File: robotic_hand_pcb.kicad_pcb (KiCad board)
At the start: 4 copper layers, 0 parts

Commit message: Fix symbol error, update component_library
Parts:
- added C1: 100n, Capacitor_SMD:C_0603_1608Metric, F.Cu at (26.0, 46.5)
- added C10: 100n, Capacitor_SMD:C_0603_1608Metric, F.Cu at (30.0, 51.5)
- added C11: 100n, Capacitor_SMD:C_0603_1608Metric, F.Cu at (30.0, 54.0)
- added C12: 100n, Capacitor_SMD:C_0603_1608Metric, F.Cu at (30.0, 56.5)
- added C13: 4u7, Capacitor_SMD:C_0603_1608Metric, F.Cu at (30.0, 59.1)
- added C14: 100n, Capacitor_SMD:C_0603_1608Metric, F.Cu at (30.0, 61.6)
- added C15: 30p, Capacitor_SMD:C_0402_1005Metric, F.Cu at (51.9, 46.2)
- added C16: 30p, Capacitor_SMD:C_0402_1005Metric, F.Cu at (51.9, 48.2)
- added C17: 2u2, Capacitor_SMD:C_0603_1608Metric, F.Cu at (34.0, 46.5)
- added C18: 18p, Capacitor_SMD:C_0402_1005Metric, F.Cu at (51.9, 50.2)
- added C19: 18p, Capacitor_SMD:C_0402_1005Metric, F.Cu at (51.9, 52.1)
- added C2: 2u2, Capacitor_SMD:C_0603_1608Metric, F.Cu at (26.0, 49.0)
- added C20: 100n, Capacitor_SMD:C_0603_1608Metric, F.Cu at (97.3, 18.1)
- added C21: 100n, Capacitor_SMD:C_0603_1608Metric, F.Cu at (97.3, 20.6)
- added C22: 18p, Capacitor_SMD:C_0402_1005Metric, F.Cu at (100.8, 31.0)
- added C23: 18p, Capacitor_SMD:C_0402_1005Metric, F.Cu at (100.8, 33.0)
- added C24: 100n, Capacitor_SMD:C_0603_1608Metric, F.Cu at (97.3, 23.1)
- added C25: 100n, Capacitor_SMD:C_0603_1608Metric, F.Cu at (70.7, 35.0)
- added C26: 100n, Capacitor_SMD:C_0603_1608Metric, F.Cu at (70.7, 37.5)
- added C27: 1u, Capacitor_SMD:C_0603_1608Metric, F.Cu at (70.7, 40.0)
- added C28: 100n, Capacitor_SMD:C_0603_1608Metric, F.Cu at (70.7, 42.5)
- added C29: 100n, Capacitor_SMD:C_0603_1608Metric, F.Cu at (70.7, 45.0)
- added C3: 22u, Capacitor_SMD:C_0603_1608Metric, F.Cu at (26.0, 51.5)
- added C30: 100n, Capacitor_SMD:C_0603_1608Metric, F.Cu at (74.7, 35.0)
- added C31: 100n, Capacitor_SMD:C_0603_1608Metric, F.Cu at (74.7, 37.5)
- added C32: 100n, Capacitor_SMD:C_0603_1608Metric, F.Cu at (74.7, 40.0)
- added C33: 1n, Capacitor_SMD:C_0603_1608Metric, F.Cu at (74.7, 42.5)
- added C34: 1n, Capacitor_SMD:C_0603_1608Metric, F.Cu at (74.7, 45.0)
- added C35: 1n, Capacitor_SMD:C_0603_1608Metric, F.Cu at (78.7, 35.0)
- added C36: 1n, Capacitor_SMD:C_0603_1608Metric, F.Cu at (78.7, 37.5)
- added C37: 1n, Capacitor_SMD:C_0603_1608Metric, F.Cu at (78.7, 40.0)
- added C38: 100n, Capacitor_SMD:C_0603_1608Metric, F.Cu at (41.3, 29.7)
- added C39: 100n, Capacitor_SMD:C_0603_1608Metric, F.Cu at (41.3, 32.2)
- added C4: 44u, Capacitor_SMD:C_0603_1608Metric, F.Cu at (26.0, 54.0)
- added C40: 100n, Capacitor_SMD:C_0603_1608Metric, F.Cu at (41.3, 34.7)
- added C41: 100n, Capacitor_SMD:C_0603_1608Metric, F.Cu at (41.3, 37.2)
- added C42: 100n, Capacitor_SMD:C_0603_1608Metric, F.Cu at (41.3, 39.7)
- added C5: 1u, Capacitor_SMD:C_0603_1608Metric, F.Cu at (26.0, 56.5)
- added C6: 2u2, Capacitor_SMD:C_0603_1608Metric, F.Cu at (26.0, 59.1)
- added C7: 100n, Capacitor_SMD:C_0603_1608Metric, F.Cu at (26.0, 61.6)
- added C8: 100n, Capacitor_SMD:C_0603_1608Metric, F.Cu at (30.0, 46.5)
- added C9: 100n, Capacitor_SMD:C_0603_1608Metric, F.Cu at (30.0, 49.0)
- added D1: WS2812B, LED_SMD:LED_WS2812B_PLCC4_5.0x5.0mm_P3.2mm, F.Cu at (95.3, 64.7)
- added D2: WS2812B, LED_SMD:LED_WS2812B_PLCC4_5.0x5.0mm_P3.2mm, F.Cu at (95.3, 71.4)
- added D3: WS2812B, LED_SMD:LED_WS2812B_PLCC4_5.0x5.0mm_P3.2mm, F.Cu at (95.3, 78.0)
- added D4: WS2812B, LED_SMD:LED_WS2812B_PLCC4_5.0x5.0mm_P3.2mm, F.Cu at (95.3, 84.6)
- added FM1: 1mm, Fiducial:Fiducial_1mm_Mask2mm, F.Cu at (37.9, 76.1)
- added FM2: 1mm, Fiducial:Fiducial_1mm_Mask2mm, F.Cu at (37.9, 79.6)
- added FM3: 1mm, Fiducial:Fiducial_1mm_Mask2mm, F.Cu at (41.4, 76.1)
- added FM4: 1mm, Fiducial:Fiducial_1mm_Mask2mm, F.Cu at (41.4, 79.6)
- added FM5: 1mm, Fiducial:Fiducial_1mm_Mask2mm, F.Cu at (45.0, 76.1)
- added FM6: 1mm, Fiducial:Fiducial_1mm_Mask2mm, F.Cu at (45.0, 79.6)
- added H1: M3, MountingHole:MountingHole_3.2mm_M3_Pad_Via, F.Cu at (20.0, 49.2)
- added H2: M3, MountingHole:MountingHole_3.2mm_M3_Pad_Via, F.Cu at (20.0, 57.2)
- added H3: M3, MountingHole:MountingHole_3.2mm_M3_Pad_Via, F.Cu at (20.0, 65.1)
- added H4: M3, MountingHole:MountingHole_3.2mm_M3_Pad_Via, F.Cu at (20.0, 73.1)
- added J1: 2171750001, common:molex_2171750001_usb_c_6p, F.Cu at (29.8, 75.8)
- added J10: A5, Connector_PinHeader_2.54mm:PinHeader_1x03_P2.54mm_Vertical, F.Cu at (81.2, 19.2)
- added J11: A6, Connector_PinHeader_2.54mm:PinHeader_1x03_P2.54mm_Vertical, F.Cu at (85.8, 19.2)
- added J12: A7, Connector_PinHeader_2.54mm:PinHeader_1x03_P2.54mm_Vertical, F.Cu at (90.5, 19.2)
- added J13: ISENSE1, Connector_PinHeader_2.54mm:PinHeader_1x02_P2.54mm_Vertical, F.Cu at (71.0, 28.9)
- added J14: ISENSE2, Connector_PinHeader_2.54mm:PinHeader_1x02_P2.54mm_Vertical, F.Cu at (75.7, 28.9)
- added J15: ISENSE3, Connector_PinHeader_2.54mm:PinHeader_1x02_P2.54mm_Vertical, F.Cu at (80.3, 28.9)
- added J16: ISENSE4, Connector_PinHeader_2.54mm:PinHeader_1x02_P2.54mm_Vertical, F.Cu at (85.0, 28.9)
- added J17: ISENSE5, Connector_PinHeader_2.54mm:PinHeader_1x02_P2.54mm_Vertical, F.Cu at (89.6, 28.9)
- added J18: JST 1x5 Male, Connector_PinHeader_2.54mm:PinHeader_1x05_P2.54mm_Vertical, F.Cu at (18.3, 30.8)
- added J19: JST 1x5 Male, Connector_PinHeader_2.54mm:PinHeader_1x05_P2.54mm_Vertical, F.Cu at (23.0, 30.8)
- added J2: TC2050-IDC, tag_connect:tag_connect_tc2050-idc, F.Cu at (41.7, 68.6)
- added J20: JST 1x5 Male, Connector_PinHeader_2.54mm:PinHeader_1x05_P2.54mm_Vertical, F.Cu at (27.6, 30.8)
- added J21: JST 1x5 Male, Connector_PinHeader_2.54mm:PinHeader_1x05_P2.54mm_Vertical, F.Cu at (32.3, 30.8)
- added J22: JST 1x5 Male, Connector_PinHeader_2.54mm:PinHeader_1x05_P2.54mm_Vertical, F.Cu at (36.9, 30.8)
- added J3: ~, common:harwin_2p_2-54_jumper_open, F.Cu at (19.7, 79.5)
- added J4: UART, Connector_PinHeader_2.54mm:PinHeader_1x02_P2.54mm_Vertical, F.Cu at (52.8, 55.5)
- added J5: WS2812B, Connector_PinHeader_2.54mm:PinHeader_1x03_P2.54mm_Vertical, F.Cu at (101.7, 63.8)
- added J6: A1, Connector_PinHeader_2.54mm:PinHeader_1x03_P2.54mm_Vertical, F.Cu at (62.6, 19.2)
- added J7: A2, Connector_PinHeader_2.54mm:PinHeader_1x03_P2.54mm_Vertical, F.Cu at (67.2, 19.2)
- added J8: A3, Connector_PinHeader_2.54mm:PinHeader_1x03_P2.54mm_Vertical, F.Cu at (71.9, 19.2)
- added J9: A4, Connector_PinHeader_2.54mm:PinHeader_1x03_P2.54mm_Vertical, F.Cu at (76.5, 19.2)
- added JP1: Open, Jumper:SolderJumper-2_P1.3mm_Open_TrianglePad1.0x1.5mm, F.Cu at (66.9, 84.6)
- added JP2: Open, Jumper:SolderJumper-2_P1.3mm_Open_TrianglePad1.0x1.5mm, F.Cu at (101.5, 28.3)
- added L1: 6u8, Resistor_SMD:R_0603_1608Metric, F.Cu at (34.0, 49.0)
- added R1: 100k, Resistor_SMD:R_0603_1608Metric, F.Cu at (34.0, 51.5)
- added R10: 2k2, Resistor_SMD:R_0603_1608Metric, F.Cu at (97.3, 35.7)
- added R2: 13k7, Resistor_SMD:R_0603_1608Metric, F.Cu at (34.0, 54.0)
- added R3: 5k1, Resistor_SMD:R_0603_1608Metric, F.Cu at (34.0, 56.5)
- added R4: 5k1, Resistor_SMD:R_0603_1608Metric, F.Cu at (34.0, 59.1)
- added R5: 10k, Resistor_SMD:R_0603_1608Metric, F.Cu at (34.0, 61.6)
- added R6: 10k, Resistor_SMD:R_0603_1608Metric, F.Cu at (97.3, 25.6)
- added R7: 10k, Resistor_SMD:R_0603_1608Metric, F.Cu at (97.3, 28.1)
- added R8: 10k, Resistor_SMD:R_0603_1608Metric, F.Cu at (97.3, 30.6)
- added R9: 2k2, Resistor_SMD:R_0603_1608Metric, F.Cu at (97.3, 33.1)
- added SW1: SPST, Button_Switch_THT:SW_PUSH_6mm, F.Cu at (48.8, 76.3)
- added TP1: TestPoint, TestPoint:TestPoint_Pad_D2.0mm, F.Cu at (82.8, 35.8)
- added TP2: TestPoint, TestPoint:TestPoint_Pad_D2.0mm, F.Cu at (82.8, 39.8)
- added TP3: TestPoint, TestPoint:TestPoint_Pad_D2.0mm, F.Cu at (82.8, 43.9)
- added TP4: TestPoint, TestPoint:TestPoint_Pad_D2.0mm, F.Cu at (82.8, 47.9)
- added TP5: TestPoint, TestPoint:TestPoint_Pad_D2.0mm, F.Cu at (82.8, 52.0)
- added U1: LMR51430, ti_buck:lmr51430, F.Cu at (27.3, 82.5)
- added U10: ACS712xLCTR-05B, Package_SO:SOIC-8_3.9x4.9mm_P1.27mm, F.Cu at (64.5, 36.5)
- added U11: ACS712xLCTR-05B, Package_SO:SOIC-8_3.9x4.9mm_P1.27mm, F.Cu at (64.5, 43.0)
- added U12: ACS712xLCTR-05B, Package_SO:SOIC-8_3.9x4.9mm_P1.27mm, F.Cu at (64.5, 49.6)
- added U13: ACS712xLCTR-05B, Package_SO:SOIC-8_3.9x4.9mm_P1.27mm, F.Cu at (64.5, 56.2)
- added U14: ULN2003ADR, Package_SO:SOIC-16_3.9x9.9mm_P1.27mm, F.Cu at (20.2, 22.7)
- added U15: ULN2003ADR, Package_SO:SOIC-16_3.9x9.9mm_P1.27mm, F.Cu at (28.7, 22.7)
- added U16: ULN2003ADR, Package_SO:SOIC-16_3.9x9.9mm_P1.27mm, F.Cu at (37.1, 22.7)
- added U17: ULN2003ADR, Package_SO:SOIC-16_3.9x9.9mm_P1.27mm, F.Cu at (45.6, 22.7)
- added U18: ULN2003ADR, Package_SO:SOIC-16_3.9x9.9mm_P1.27mm, F.Cu at (54.0, 22.7)
- added U2: ld39150dt33-r, common:to-252-2_dpak-2-leg, F.Cu at (30.9, 66.9)
- added U3: TXB0104QPWRQ1, common:txb0104qpwrq1, F.Cu at (51.5, 66.2)
- added U4: STM32F446RET, Package_QFP:LQFP-64_10x10mm_P0.5mm, F.Cu at (43.2, 52.5)
- added U5: VL53L4CD, time_of_flight:vl53l4cd_lga12, F.Cu at (62.3, 85.8)
- added U6: ~, adafruit:adafruit_5396_vl53l4cd, F.Cu at (74.7, 72.1)
- added U7: BNO085, ceva:bno085, F.Cu at (101.9, 20.1)
- added U8: ADS114S08, adc:ads114s08_tqfp-32, F.Cu at (89.1, 38.0)
- added U9: ACS712xLCTR-05B, Package_SO:SOIC-8_3.9x4.9mm_P1.27mm, F.Cu at (64.5, 29.9)
- added Y1: 8M, common:ecs_ecx-64, F.Cu at (51.6, 71.7)
- added Y2: 32k768, common:ecs_ecx-34r, F.Cu at (33.0, 81.8)
- added Y3: 32k768, common:ecs_ecx-34r, F.Cu at (102.3, 24.9)

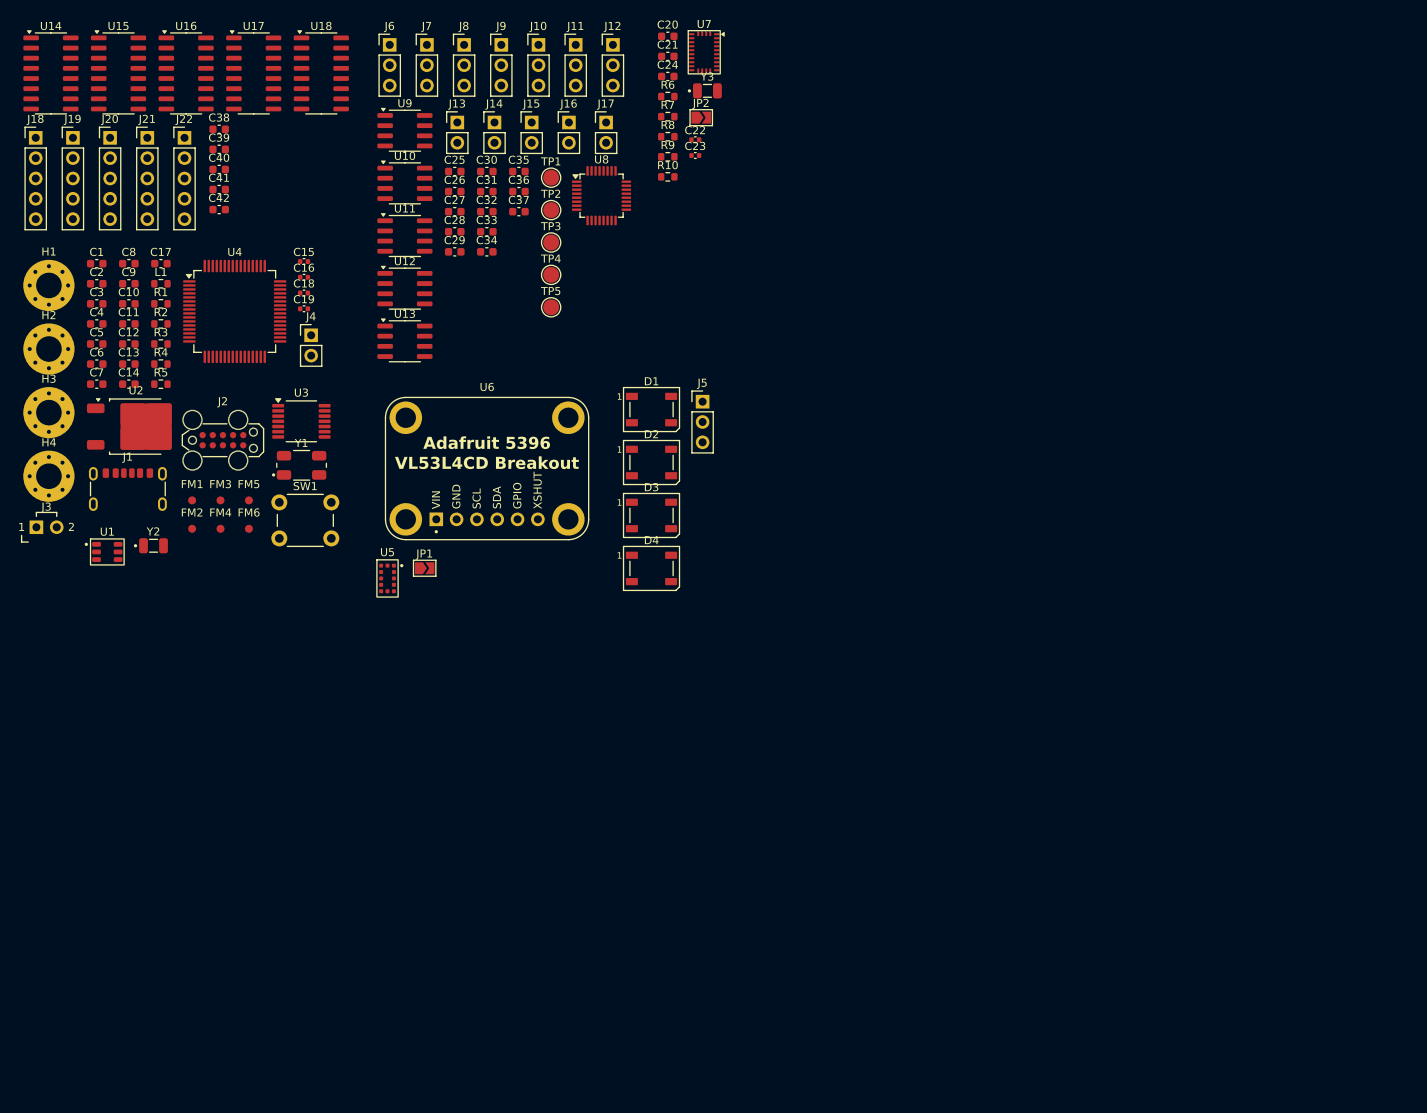
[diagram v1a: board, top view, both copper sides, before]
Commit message: Add WIP PCB layout and routing
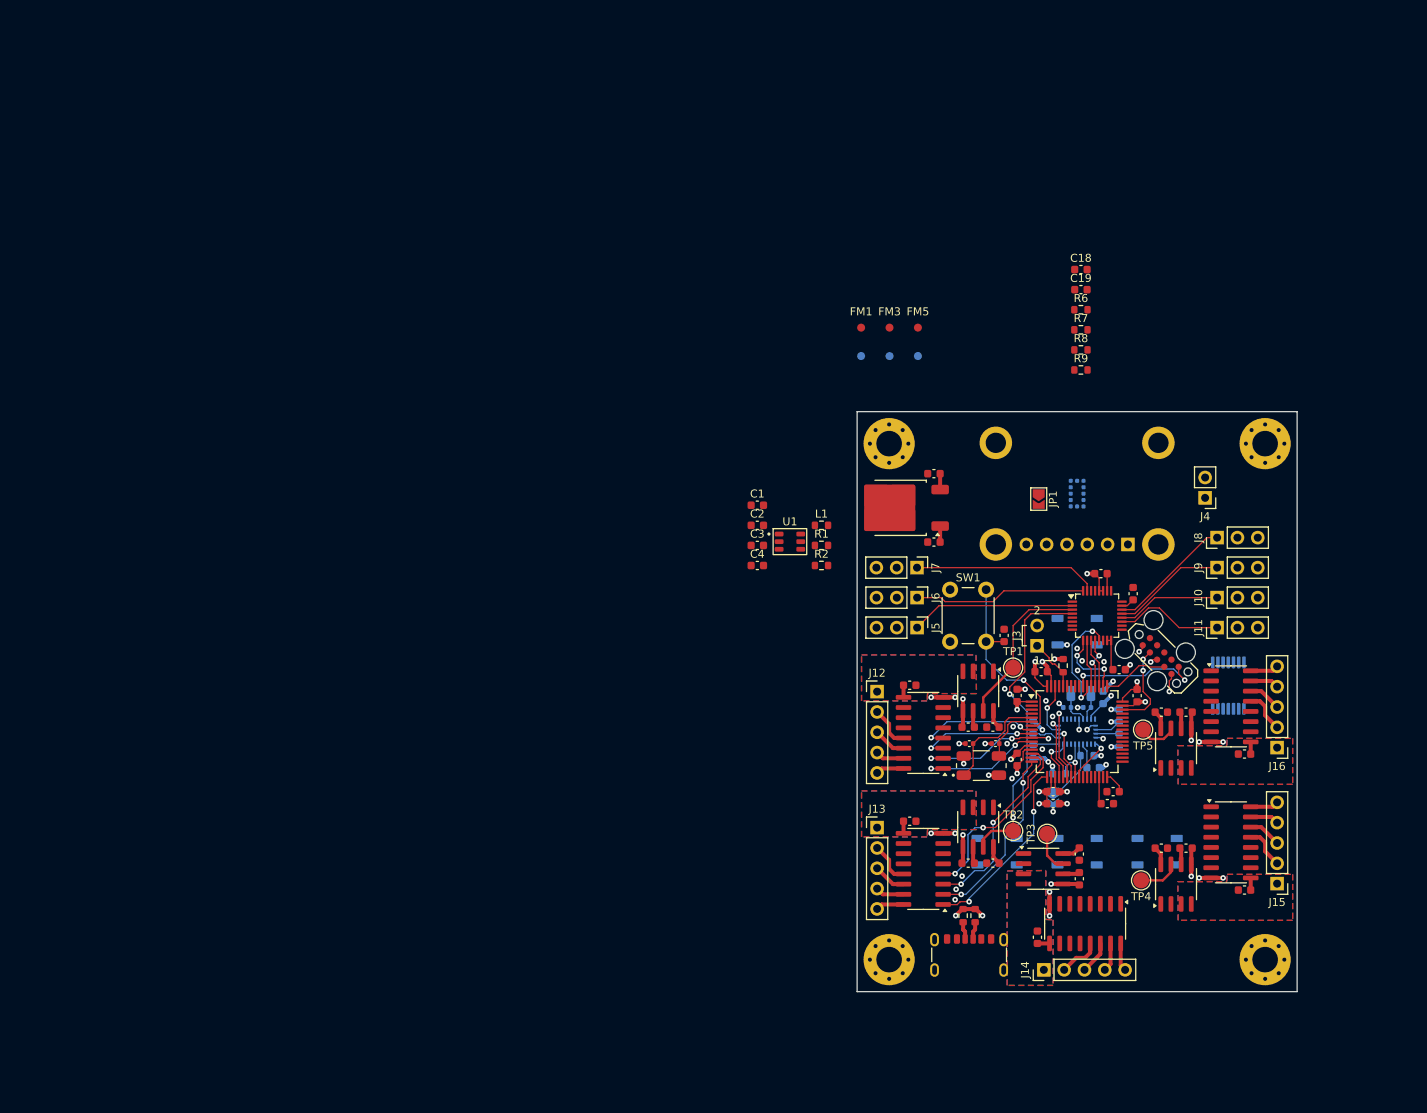
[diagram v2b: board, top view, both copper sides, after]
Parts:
- removed the C38 at (41.3, 29.7)
- removed J17: ISENSE5, Connector_PinHeader_2.54mm:PinHeader_1x02_P2.54mm_Vertical
- removed J18, J19, J20, J21: JST 1x5 Male, Connector_PinHeader_2.54mm:PinHeader_1x05_P2.54mm_Vertical
- removed the J5 at (101.7, 63.8)
- removed the U14 at (20.2, 22.7)
- removed the Y2 at (33.0, 81.8)
- added C42: 100n, Capacitor_SMD:C_0603_1608Metric, F.Cu at (169.4, 107.8)
- added R6: 2k2, Resistor_SMD:R_0603_1608Metric, F.Cu at (149.0, 52.3)
- added R7: 2k2, Resistor_SMD:R_0603_1608Metric, F.Cu at (149.0, 54.8)
- added R8: 2k2, Resistor_SMD:R_0603_1608Metric, F.Cu at (149.0, 57.3)
- added R9: 2k2, Resistor_SMD:R_0603_1608Metric, F.Cu at (149.0, 59.8)
- added U18: ULN2003ADR, Package_SO:SOIC-16_3.9x9.9mm_P1.27mm, F.Cu at (167.7, 101.8)
- C18: value 18p -> 100n; footprint Capacitor_SMD:C_0402_1005Metric -> Capacitor_SMD:C_0603_1608Metric
- C19: value 18p -> 4u7; footprint Capacitor_SMD:C_0402_1005Metric -> Capacitor_SMD:C_0603_1608Metric
- C20, C21, C22, C23, C24, D1, D2, D3, D4, FM2, FM4, FM6, JP2, U3, U5, U6, U7: moved to B.Cu
- J10: renamed from J12; value A7 -> A6
- J11: value A6 -> A7
- J13: value ISENSE1 -> JST 1x5 Male; footprint Connector_PinHeader_2.54mm:PinHeader_1x02_P2.54mm_Vertical -> Connector_PinHeader_2.54mm:PinHeader_1x05_P2.54mm_Vertical
- J14: value ISENSE2 -> JST 1x5 Male; footprint Connector_PinHeader_2.54mm:PinHeader_1x02_P2.54mm_Vertical -> Connector_PinHeader_2.54mm:PinHeader_1x05_P2.54mm_Vertical
- J15: value ISENSE3 -> JST 1x5 Male; footprint Connector_PinHeader_2.54mm:PinHeader_1x02_P2.54mm_Vertical -> Connector_PinHeader_2.54mm:PinHeader_1x05_P2.54mm_Vertical
- J16: value ISENSE4 -> JST 1x5 Male; footprint Connector_PinHeader_2.54mm:PinHeader_1x02_P2.54mm_Vertical -> Connector_PinHeader_2.54mm:PinHeader_1x05_P2.54mm_Vertical
- R10: renamed from R6; moved to B.Cu
- R11: renamed from R7; moved to B.Cu
- R12: renamed from R8; moved to B.Cu
- R13: renamed from R9; moved to B.Cu
- R14: renamed from R10; moved to B.Cu
- Y2: renamed from Y3; moved to B.Cu
- moved H3 166.7 mm to (172.0, 133.5)
- moved U17 155.4 mm to (167.7, 118.8)
- moved C41 155.2 mm to (169.4, 124.8), turned to 180 degrees
- moved U16 154.7 mm to (149.5, 129.0), turned to -90 degrees
- moved H2 152.5 mm to (172.0, 69.0)
- moved U15 141.4 mm to (129.3, 122.2), turned to 180 degrees
- moved C40 140.3 mm to (143.5, 130.7), turned to 90 degrees
- moved C9 138.4 mm to (153.0, 112.5), turned to 180 degrees
- moved C17 136.2 mm to (152.3, 114.0)
- moved C10 135.2 mm to (156.0, 100.5), turned to -90 degrees
- moved J15 133.2 mm to (173.5, 124.0), turned to 180 degrees
- moved C8 133.1 mm to (145.5, 112.5), turned to 180 degrees
- moved C13 127.9 mm to (145.5, 114.0), turned to 180 degrees
- moved J14 126.2 mm to (144.3, 134.8), turned to 90 degrees
- moved J3 124.6 mm to (143.5, 93.0), turned to 90 degrees
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- renumbered C42 to C38, J22 to J12, J6 to J5, J7 to J6, J8 to J7, J9 to J8, J10 to J9, U18 to U14
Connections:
- C18 pad 1: /LSE_IN -> +3V3
- C19 pad 1: /LSE_OUT -> +3V3
- D4 pad 2: Net-(D4-DOUT) -> unconnected-(D4-DOUT-Pad2)
- J10 pad 1: /robotic_hand_pcb_analog/ADC12 -> /robotic_hand_pcb_analog/ADC11
- J11 pad 1: /robotic_hand_pcb_analog/ADC11 -> /robotic_hand_pcb_analog/ADC12
- J12 pad 2: Net-(J22-Pin_2) -> Net-(J12-Pin_2)
- J12 pad 3: Net-(J22-Pin_3) -> Net-(J12-Pin_3)
- J12 pad 4: Net-(J22-Pin_4) -> Net-(J12-Pin_4)
- J12 pad 5: Net-(J22-Pin_5) -> Net-(J12-Pin_5)
- J13 pad 2: +5V -> Net-(J13-Pin_2)
- J14 pad 2: +5V -> Net-(J14-Pin_2)
- J15 pad 2: +5V -> Net-(J15-Pin_2)
- J16 pad 2: +5V -> Net-(J16-Pin_2)
- U14 pad 1: /M5_1 -> /M1_1
- U14 pad 13: Net-(J22-Pin_5) -> Net-(J12-Pin_2)
- U14 pad 14: Net-(J22-Pin_4) -> Net-(J12-Pin_3)
- U14 pad 15: Net-(J22-Pin_3) -> Net-(J12-Pin_4)
- U14 pad 16: Net-(J22-Pin_2) -> Net-(J12-Pin_5)
- U14 pad 2: /M5_2 -> /M1_2
- U14 pad 3: /M5_3 -> /M1_3
- U14 pad 4: /M5_4 -> /M1_4
- U15 pad 1: /M2_1 -> /M3_1
- U15 pad 13: Net-(J19-Pin_5) -> Net-(J13-Pin_2)
- U15 pad 14: Net-(J19-Pin_4) -> Net-(J13-Pin_3)
- U15 pad 15: Net-(J19-Pin_3) -> Net-(J13-Pin_4)
- U15 pad 16: Net-(J19-Pin_2) -> Net-(J13-Pin_5)
- U15 pad 2: /M2_2 -> /M3_2
- U15 pad 3: /M2_3 -> /M3_3
- U15 pad 4: /M2_4 -> /M3_4
- U16 pad 1: /M3_1 -> /M4_1
- U16 pad 13: Net-(J20-Pin_5) -> Net-(J14-Pin_2)
- U16 pad 14: Net-(J20-Pin_4) -> Net-(J14-Pin_3)
- U16 pad 15: Net-(J20-Pin_3) -> Net-(J14-Pin_4)
- U16 pad 16: Net-(J20-Pin_2) -> Net-(J14-Pin_5)
- U16 pad 2: /M3_2 -> /M4_2
- U16 pad 3: /M3_3 -> /M4_3
- U16 pad 4: /M3_4 -> /M4_4
- U17 pad 1: /M4_1 -> /M5_1
- U17 pad 13: Net-(J21-Pin_5) -> Net-(J15-Pin_2)
- U17 pad 14: Net-(J21-Pin_4) -> Net-(J15-Pin_3)
- U17 pad 15: Net-(J21-Pin_3) -> Net-(J15-Pin_4)
- U17 pad 16: Net-(J21-Pin_2) -> Net-(J15-Pin_5)
- U17 pad 2: /M4_2 -> /M5_2
- U17 pad 3: /M4_3 -> /M5_3
- U17 pad 4: /M4_4 -> /M5_4
- U4 pad 10: /M1_3 -> /M1_2
- U4 pad 11: /M1_4 -> /M1_1
- U4 pad 14: /M3_1 -> /M3_4
- U4 pad 15: /M3_2 -> /M3_3
- U4 pad 16: /M3_3 -> /M3_2
- U4 pad 17: /EXTI3_IMU_INT -> /M3_1
- U4 pad 20: /GPIO_SPI1_CS -> /EXTI4_IMU_INT
- U4 pad 26: /M3_4 -> /M4_4
- U4 pad 27: /M4_1 -> /M4_3
- U4 pad 29: unconnected-(U4-PB10-Pad29) -> /M4_1
- U4 pad 3: /LSE_IN -> unconnected-(U4-PC14_OSC32_LSE_IN-Pad3)
- U4 pad 33: /M5_1 -> /M5_4
- U4 pad 34: /M5_2 -> /M5_3
- U4 pad 35: /M5_3 -> /M5_2
- U4 pad 36: /M5_4 -> /M5_1
- U4 pad 37: /M2_1 -> /M2_4
- U4 pad 38: /M2_2 -> /M2_3
- U4 pad 39: /M2_3 -> /M2_2
- U4 pad 4: /LSE_OUT -> unconnected-(U4-PC15_OSC32_LSE_OUT-Pad4)
- U4 pad 40: /M2_4 -> /M2_1
- U4 pad 61: /M4_3 -> unconnected-(U4-PB8-Pad61)
- U4 pad 62: /M4_4 -> /GPIO_SPI1_CS
- U4 pad 8: /M1_1 -> /M1_4
- U4 pad 9: /M1_2 -> /M1_3
- U7 pad 14: /EXTI3_IMU_INT -> /EXTI4_IMU_INT
- U8 pad 3: /robotic_hand_pcb_analog/ADC5 -> /robotic_hand_pcb_analog/ADC1
- U8 pad 4: /robotic_hand_pcb_analog/ADC4 -> /robotic_hand_pcb_analog/ADC2
- U8 pad 6: /robotic_hand_pcb_analog/ADC2 -> /robotic_hand_pcb_analog/ADC4
- U8 pad 7: /robotic_hand_pcb_analog/ADC1 -> /robotic_hand_pcb_analog/ADC5
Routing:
- net GND: track 0.00 -> 76.1 mm, vias 0 -> 55
- net +3V3: track 0.00 -> 44.6 mm, vias 0 -> 15
- net /robotic_hand_pcb_analog/ADC2: track 0.00 -> 40.2 mm, vias 0 -> 2
- net /NRST: track 0.00 -> 24.2 mm, vias 0 -> 1
- net /M3_3: track 0.00 -> 23.8 mm, vias 0 -> 2
- net /M3_4: track 0.00 -> 23.6 mm, vias 0 -> 2
- net /M3_1: track 0.00 -> 23.4 mm, vias 0 -> 2
- net +5V: track 0.00 -> 23.3 mm
- net /robotic_hand_pcb_analog/ADC8: track 0.00 -> 23.0 mm
- net /M3_2: track 0.00 -> 22.8 mm, vias 0 -> 2
- net /robotic_hand_pcb_analog/ADC7: track 0.00 -> 21.5 mm
- net /robotic_hand_pcb_analog/ADC6: track 0.00 -> 20.5 mm
- net /robotic_hand_pcb_analog/ADC1: track 0.00 -> 20.4 mm
- net /M1_2: track 0.00 -> 17.4 mm, vias 0 -> 3
- net /SWO: track 0.00 -> 16.9 mm, vias 0 -> 2
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- added copper zone on B.Cu, net +5V
- added copper zone on F.Cu, net +5V
- added copper zone on In1.Cu, net GND
- added copper zone on In2.Cu, net GND
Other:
- board outline added: 55 x 72.5 mm

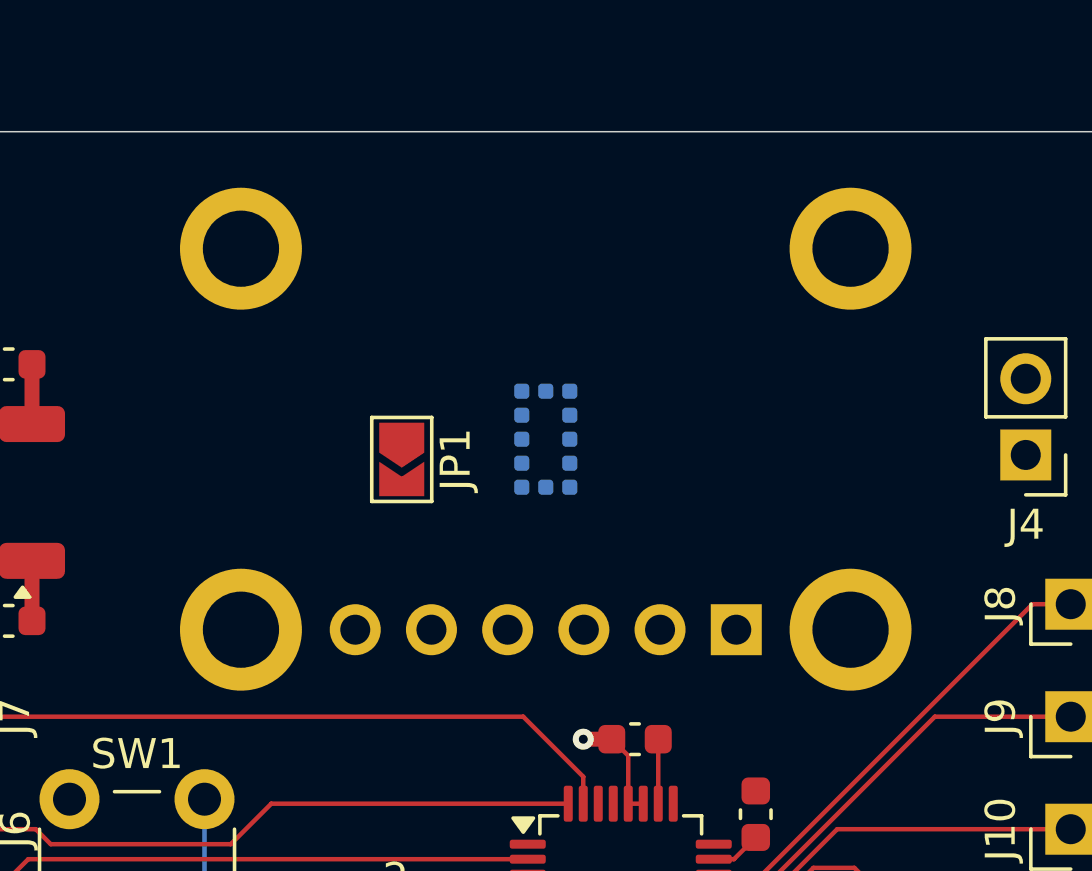
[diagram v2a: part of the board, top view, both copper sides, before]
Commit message: Swap adafruit breakout for pin header footprint
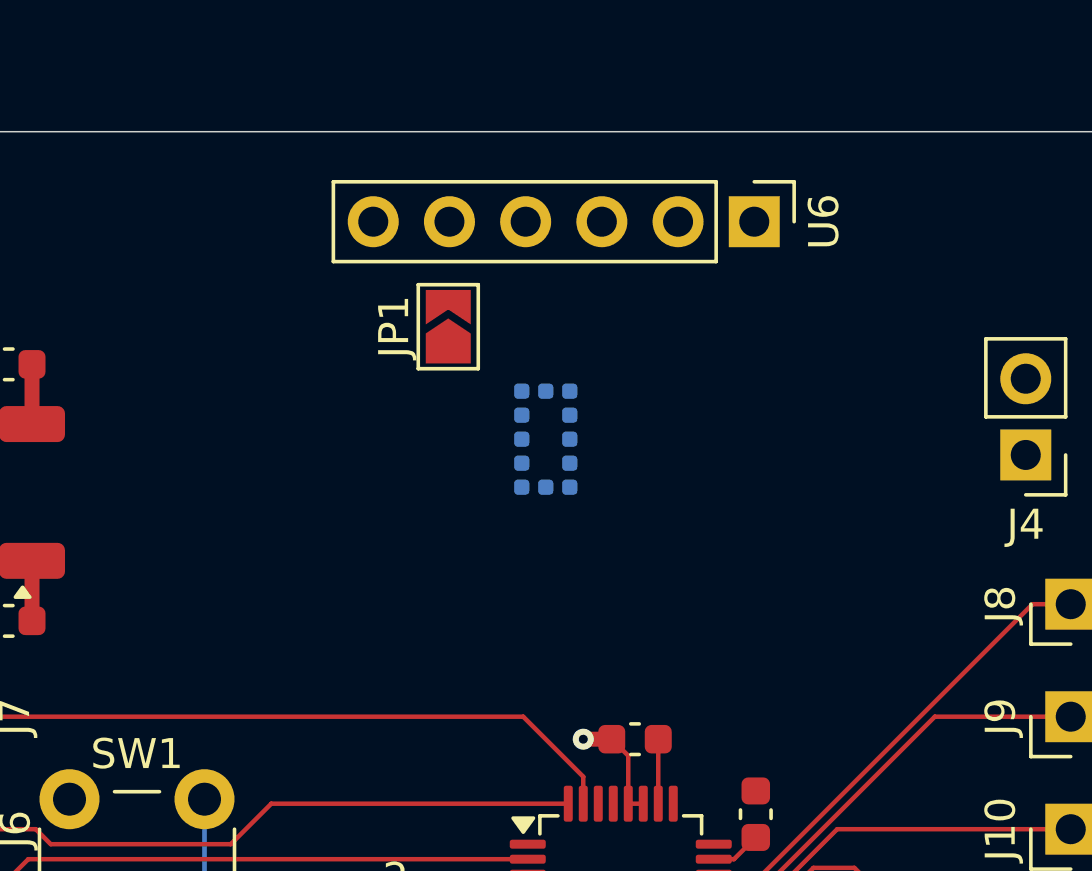
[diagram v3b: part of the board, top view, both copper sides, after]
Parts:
- U6: footprint adafruit:adafruit_5396_vl53l4cd -> Connector_PinHeader_2.54mm:PinHeader_1x06_P2.54mm_Vertical; moved to F.Cu
- moved U6 10.0 mm to (155.4, 68.0), turned to -90 degrees
- moved JP1 4.69 mm to (145.2, 71.5), turned to 90 degrees
